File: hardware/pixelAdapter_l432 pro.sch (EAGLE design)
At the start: 36 parts, among them U1 SN74HCT245PWR, U2 AP2120N-3.3TRG1, U3 STM32L432KCU6

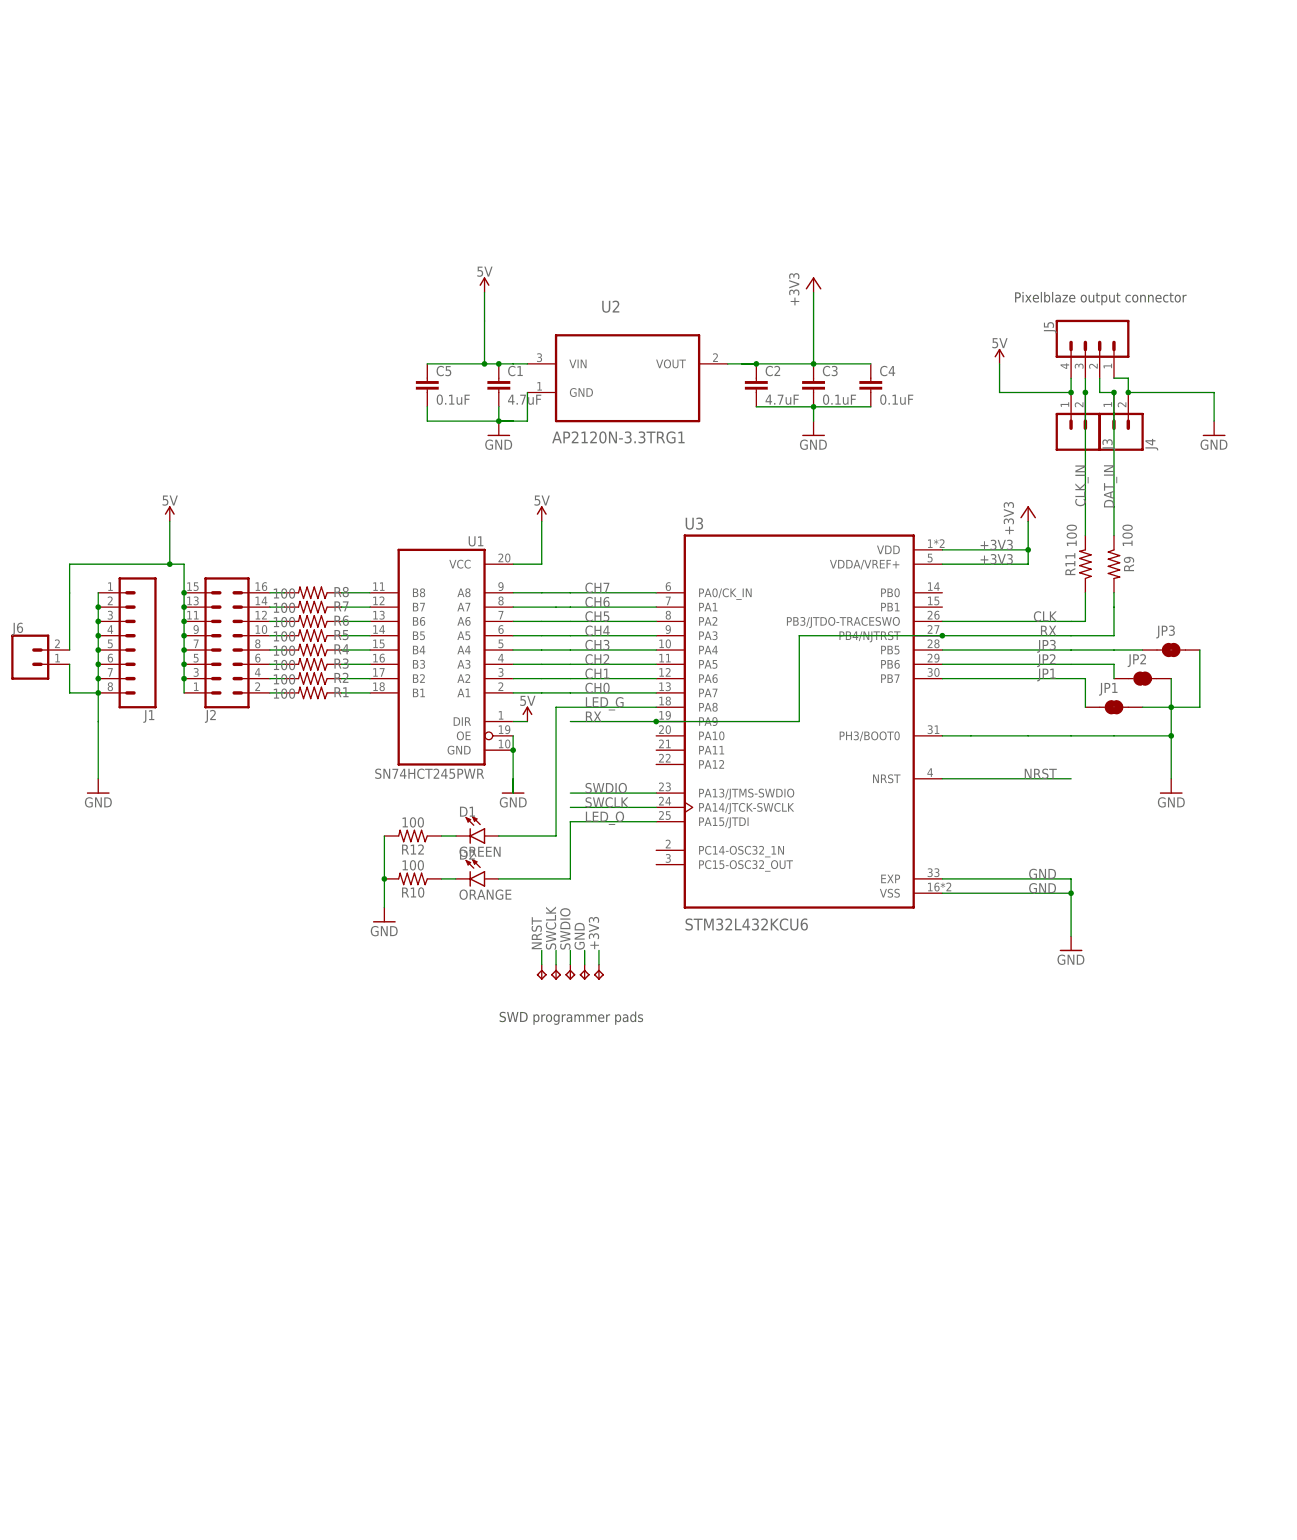
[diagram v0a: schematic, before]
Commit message: hardware files for variants, limit max transfer bits
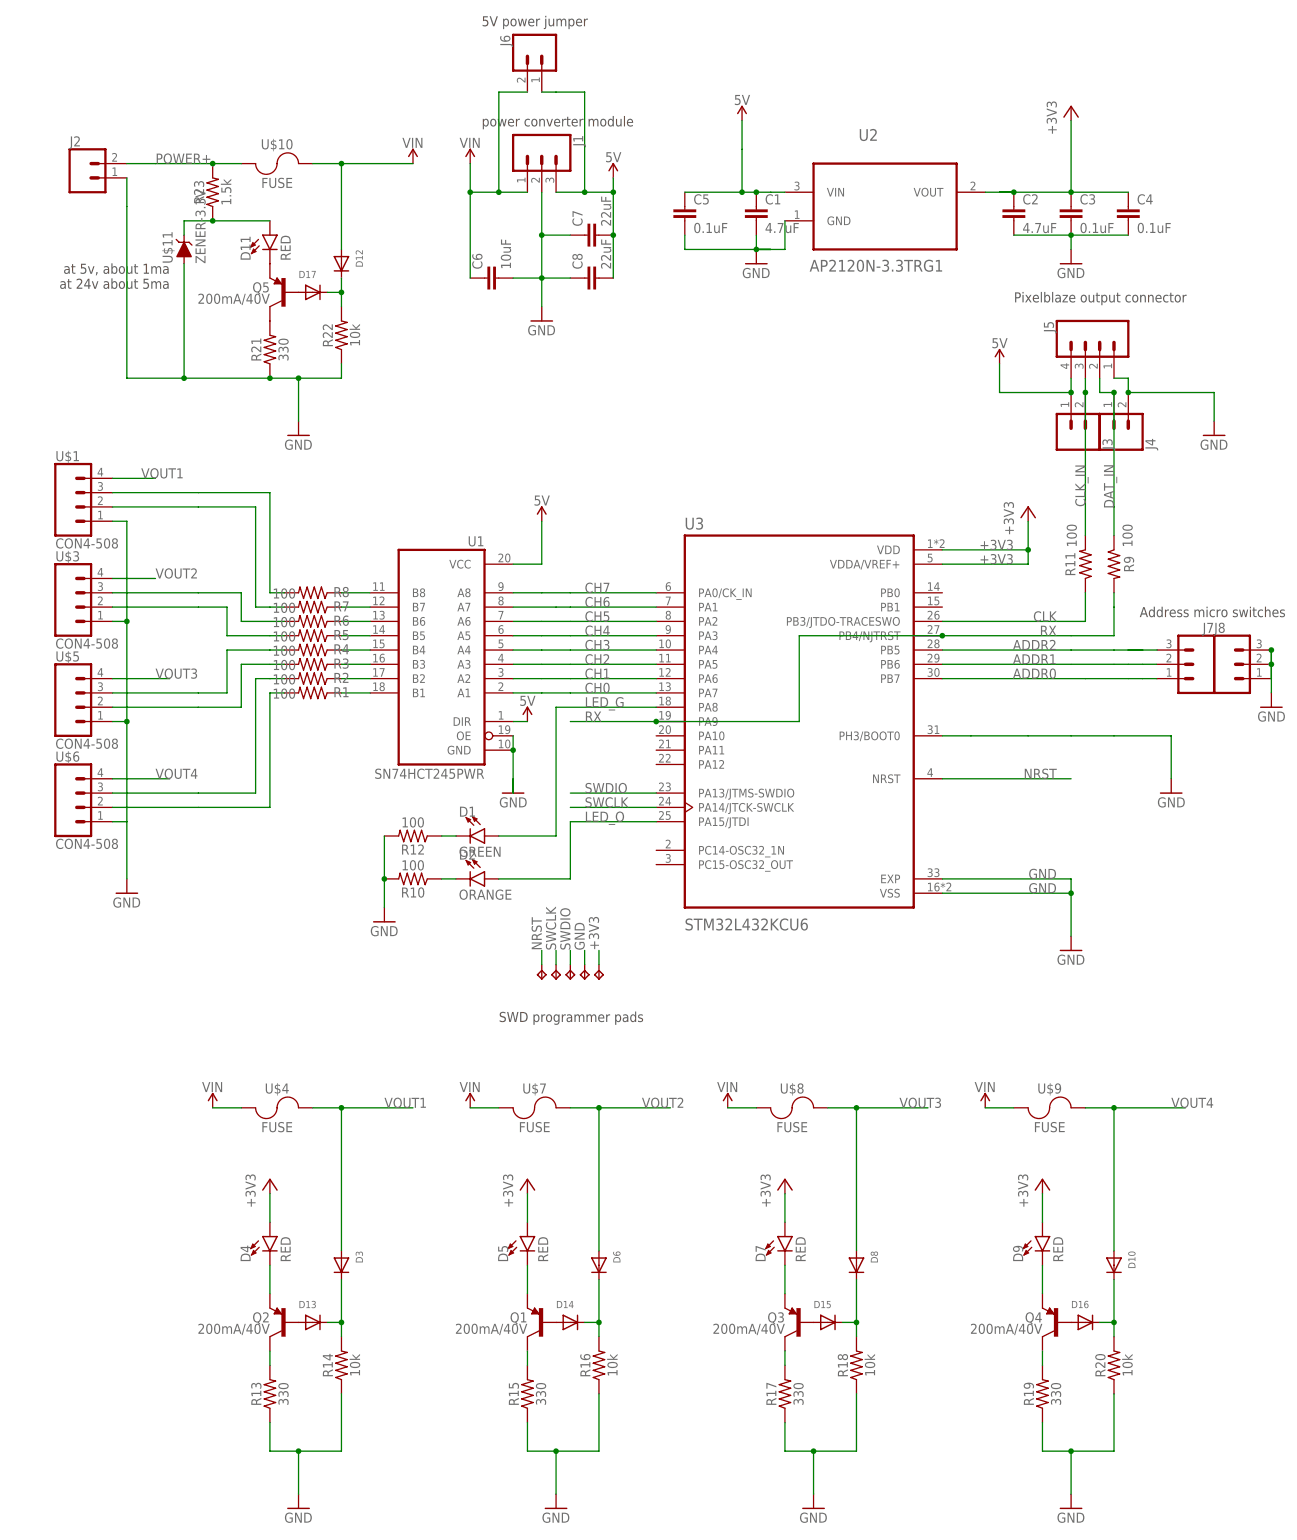
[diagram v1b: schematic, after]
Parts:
- removed JP1, JP2, JP3: JUMPER-SMT_2_NC_TRACE_SILK, SparkFun-Jumpers:JUMPER-SMT_2_NC_TRACE_SILK
- added C6: 10uF, SparkFun-Capacitors:10UF-1210-50V-20%
- added C7, C8: 22uF, SparkFun-Capacitors:22UF-1210-16V-20%
- added D10, D12, D13, D14, D15, D16, D17, D3, D6, D8: (no value), adafruit:DIODESOD-123
- added D11, D4, D5, D7, D9: RED, SparkFun-LED:LED-RED0603
- added J7, J8: (no value), SparkFun-Connectors:CONN_03LOCK
- added Q1, Q2, Q3, Q4, Q5: 200mA/40V, SparkFun-DiscreteSemi:TRANS_PNP-PMBT3906|MMBT3906L
- added R13, R15, R17, R19, R21: 330, SparkFun-Resistors:RESISTOR0603
- added R14, R16, R18, R20, R22: 10k, SparkFun-Resistors:10KOHM-0603-1/10W-1%
- added R23: 1.5k, SparkFun-Resistors:1.5KOHM-0603-1/10W-1%
- added U$1, U$3, U$5, U$6: CON4-508, bens:CON4-508
- added U$10, U$4, U$7, U$8, U$9: FUSE, bens:FUSE
- added U$11: ZENER-3.3V, bens:ZENER
- J1: device SparkFun-Connectors:CONN_08NO_SILK_FEMALE_PTH -> SparkFun-Connectors:CONN_03
- J2: device bens:CONN_08X2NOSILK -> bens:CONN_025MM
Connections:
- removed net JP1: JP1.1, U3.PB7
- removed net JP2: JP2.1, U3.PB6
- removed net JP3: JP3.2, U3.PB5
- new net ADDR0: J7.1, U3.PB7
- new net ADDR1: J7.2, U3.PB6
- new net ADDR2: J7.3, U3.PB5
- new net N$1: D17.A, Q5.B
- new net N$10: D5.C, Q1.E
- new net N$11: Q1.C, R15.2
- new net N$20: D11.A, R23.1, U$11.C
- new net N$22: D15.C, D8.C, R18.2
- new net N$23: D7.C, Q3.E
- new net N$24: Q3.C, R17.2
- new net N$25: D13.A, Q2.B
- new net N$26: D10.C, D16.C, R20.2
- new net N$27: D9.C, Q4.E
- new net N$28: Q4.C, R19.2
- new net N$29: D14.A, Q1.B
- new net N$3: D12.C, D17.C, R22.2
- new net N$30: D15.A, Q3.B
- new net N$31: D16.A, Q4.B
- new net N$4: D13.C, D3.C, R14.2
- new net N$5: D4.C, Q2.E
- new net N$6: D11.C, Q5.E
- new net N$7: Q2.C, R13.2
- new net N$8: Q5.C, R21.2
- new net N$9: D14.C, D6.C, R16.2
- new net POWER+: J2.2, R23.2, U$10.1
- new net VIN: C6.1, D12.A, J1.1, J6.2, U$10.2, U$4.1, U$7.1, U$8.1, U$9.1
- new net VOUT1: D3.A, U$1.4, U$4.2
- new net VOUT2: D6.A, U$3.4, U$7.2
- new net VOUT3: D8.A, U$5.4, U$8.2
- new net VOUT4: D10.A, U$6.4, U$9.2
- net +3V3: now also D4.A, D5.A, D7.A, D9.A
- net 5V: now also C7.2, C8.2, J1.3, J6.1; no longer J2.1, J2.11, J2.13, J2.15, J2.3, J2.5, J2.7, J2.9, J6.2
- net GND: now also C6.2, C7.1, C8.1, J2.1, J8.1, J8.2, J8.3, R13.1, R14.1, R15.1, R16.1, R17.1, R18.1, R19.1, R20.1, R21.1, R22.1, U$1.1, U$11.A, U$3.1, U$5.1, U$6.1; no longer J1.1, J1.3, J1.4, J1.5, J1.6, J1.7, J1.8, J6.1, JP1.2, JP2.2, JP3.1
- net LED0: now also U$6.2; no longer J2.2
- net LED1: now also U$6.3; no longer J2.4
- net LED2: now also U$5.2; no longer J2.6
- net LED3: now also U$5.3; no longer J2.8
- net LED4: now also U$3.2; no longer J2.10
- net LED5: now also U$3.3; no longer J2.12
- net LED6: now also U$1.2; no longer J2.14
- net LED7: now also U$1.3; no longer J2.16
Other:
- note added: "5V power jumper"
- note added: "Address micro switches"
- note added: "at 5v, about 1ma at 24v about 5ma"
- note added: "power converter module"
- moved on the sheet: C1, C2, C3, C4, C5, J6, U2
